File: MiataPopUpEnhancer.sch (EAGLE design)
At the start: 40 parts, among them J3 USB4110-GF-A, Q1 MICRO_COMMERCIAL_MMSS8050-L-T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, Q11 MICRO_COMMERCIAL_MMSS8050-L-T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, Q12 MICRO_COMMERCIAL_MMSS8050-L-T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, Q13 DIODES_INC_DMP3099L-13DIODES_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, Q2 MICRO_COMMERCIAL_MMSS8050-L-T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, Q3 DIODES_INC_DMP3099L-13DIODES_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, SW1 KMR2, U1 ATSAMD21E18A-MUT, U2 MCP1703CB

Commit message: Adds BLE module Adds Motor indicator sense circuitry Simplifies INPUT circuitry for UP/DOWN requests Adds circuit protections
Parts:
- removed J15, J5: (no value), jumper:SJ
- removed J4: (no value), jumper:SJ2W
- added C21, C31, C6: 1uF, adafruit:C-USC0603
- added D13, D23, D3, D33: 3.3V, diode:BZX84CSMD
- added D21, D31: BAT54S, diode:BAT54S
- added D4: BAT54C, diode:BAT54C
- added D5, D6, D7: (no value), adafruit:LEDCHIPLED_0603
- added J22: (no value), adafruit:PINHD-1X6LOCK
- added Q21, Q22, Q31, Q32: MICRO_COMMERCIAL_MMSS8050-L-TPMICRO_COMMERCIAL_MMSS8050-L-T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, Micro Commercial - MMSS8050-L-TP - Copy:MICRO_COMMERCIAL_MMSS8050-L-TPMICRO_COMMERCIAL_MMSS8050-L-TP_0_0
- added Q23, Q33: DIODES_INC_DMP3099L-13DIODES_INC_DMP3099L-13_0_2, Diodes Inc. - DMP3099L-13:DIODES_INC_DMP3099L-13DIODES_INC_DMP3099L-13_0_2
- added R21, R22, R24, R31, R32, R33, R34, R41, R44, R45, S23: 2.2k, rcl:R-US_R0603
- added R25, R35, R42, R43: 100k, rcl:R-US_R0603
- added R26, R36: 1k, rcl:R-US_R0603
- added S1, S11, S21, S31: (no value), jumper:SJ
- added TVS1, TVS2, TVS3, TVS4: ESDU02A5V5R17V, ESDU02A5V5R17V:ESDU02A5V5R17V
- added U3: MDBT40, MDBT40_210701:MDBT40
- added Y1: ABS25-32.768KHZ-T, adafruit:CRYSTALMM20SS
- C1, C11, C4: value 100nF -> 1uF
- D2: value BAT54S -> BAT54C; device diode:BAT54S -> diode:BAT54C
- J1, J2: device adafruit:PINHD-1X8LOCK -> adafruit:PINHD-1X6LOCK
- R1, R11, R12, R2: value 100k -> 2.2k
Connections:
- net DOWN_OUT renamed DOWN_OUT_LH_12V
- removed net +5V: D2.C1A2, J3.VBUS, J3.VBUS_2
- removed net DOWN_OUT_3V3: R14.1
- removed net DOWN_SW: D11.C1A2, J1.5, J15.2, R11.1
- removed net DOWN_SW_3V3: J15.1, Q11.C, R13.1
- removed net DOWN_SW_FILT: C11.1, Q11.B, R11.2, R12.2
- removed net HAZARD: J1.7, J2.7
- removed net LIGHT1: J1.1, J2.1
- removed net LIGHT2: J1.2, J2.2
- removed net UP_OUT: J2.3, Q3.D
- removed net UP_OUT_3V3: R4.1
- removed net UP_SW: D1.C1A2, J1.3, J5.2, R1.1
- removed net UP_SW_3V3: J5.1, Q1.C, R3.1
- removed net UP_SW_FILT: C1.1, Q1.B, R1.2, R2.2
- new net BLE_CONNECTED: R45.1, U3.P0.19
- new net BLE_CTS: R43.1, U1.PA08, U3.P0.10
- new net BLE_MODE: U1.PA02, U3.P0.01
- new net BLE_MODE_LED: R44.1, U3.P0.18
- new net BLE_RTS: U1.PA09, U3.P0.08
- new net BLE_RXD: R42.1, U1.PA06, U3.P0.11
- new net BLE_TXD: U1.PA07, U3.P0.09
- new net DASH_IND_12V: D2.CC, J1.1
- new net DASH_IND_LH: Q21.C, S21.1, S23.1, U1.PA14
- new net DASH_IND_LH_12V: D2.A1, D21.C1A2, J2.1, R21.1
- new net DASH_IND_LH_FILT: C21.1, D23.C, Q21.B, R21.2, R22.2, S21.2
- new net DASH_IND_RH: Q31.C, R33.1, S31.1, U1.PA15
- new net DASH_IND_RH_12V: D2.A2, D31.C1A2, J22.1, R31.1
- new net DASH_IND_RH_FILT: C31.1, D33.C, Q31.B, R31.2, R32.2, S31.2
- new net DEBUG_LED: R41.1, U1.PA10
- new net DOWN_OUT_LH: R14.1, U1.PA18
- new net DOWN_OUT_RH: R34.1, U1.PA16
- new net DOWN_OUT_RH_12V: J22.5, Q33.D
- new net DOWN_REQ: Q11.C, R13.1, S11.1, U1.PA22
- new net DOWN_REQ_12V: D11.C1A2, J1.5, R11.1
- new net DOWN_REQ_FILT: C11.1, D13.C, Q11.B, R11.2, R12.2, S11.2
- new net N$10: Q32.C, Q33.G, R36.1
- new net N$11: Q32.B, R34.2, R35.2
- new net N$12: U3.P0.26/XL2, Y1.2
- new net N$13: U3.P0.27/XL1, Y1.1
- new net N$14: D5.A, R44.2
- new net N$15: D6.A, R45.2
- new net N$16: D7.A, R41.2
- new net N$8: Q22.B, R24.2, R25.2
- new net NC_BLE_FCTRYRST: U3.P0.16
- new net NC_BLE_SWCLK: U3.SWCLK
- new net NC_BLE_SWDIO/RST: U3.NRESET/SWDIO
- new net UP_OUT_LH: R4.1, U1.PA19
- new net UP_OUT_LH_12V: J2.2, Q3.D
- new net UP_OUT_RH: R24.1, U1.PA17
- new net UP_OUT_RH_12V: J22.2, Q23.D
- new net UP_REQ: Q1.C, R3.1, S1.1, U1.PA23
- new net UP_REQ_12V: D1.C1A2, J1.2, R1.1
- new net UP_REQ_FILT: C1.1, D3.C, Q1.B, R1.2, R2.2, S1.2
- new net VBUS: D4.A1, J3.VBUS, J3.VBUS_2, TVS1.2
- new net VIN: C2.1, D4.CC, U2.VI
- net +12V: now also D21.C2, D31.C2, D4.A2, J1.4, J2.4, J22.4, Q23.S, Q33.S, R26.2, R36.2, TVS4.1; no longer C2.1, D2.C2, J2.6, J4.1, U2.VI
- net +3V3: now also C6.1, R33.2, R35.1, R42.2, R43.2, S23.2, U3.AVDD, U3.VDD; no longer J4.3
- net GND: now also C21.2, C31.2, C6.2, D13.A, D21.A1, D23.A, D3.A, D31.A1, D33.A, D5.C, D6.C, D7.C, J1.3, J2.3, J22.3, Q21.E, Q22.E, Q31.E, Q32.E, R22.1, R25.1, R32.1, TVS1.1, TVS2.1, TVS3.1, TVS4.2, U3.GND@1, U3.GND@13, U3.GND@2, U3.GND@25, U3.GND@42, U3.P0.30; no longer J1.8, J2.8
- net N$7: now also Q22.C, Q23.G, R26.1; no longer J1.6, J4.2
- net USB_D+: now also TVS2.2
- net USB_D-: now also TVS3.2
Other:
- note added: "- Figure out wire harness - Determine correct PU/PD polarity for R5 and R15 - Find proper connectors for J1 and J2"
- note added: "1. Zener based: - Populate Dx3 - Nostuff Qx1 and Rx3 - Short Sx1 2. Transistor based (inverted) - Nostuff Dx3 - Populate Qx1 and Rx3 - Open Sx1"
- note added: "BLE module"
- note added: "DASH_IND_LH/RH"
- note added: "From headlight motors"
- note added: "Left"
- note added: "Motor indicators sense"
- note added: "Power regulation"
- note added: "Right"
- note added: "Rx1Cx1 = Rx2Cx1 ~= 2ms"
- note added: "SAMD21 MCU"
- note added: "To Left headlight motor"
- note added: "To Left headlight motor relay"
- note added: "To Right headlight motor"
- note added: "To dash light"
- note added: "UP/DOWN dash switch sense"
- note added: "UP/DOWN_OUT_LH"
- note added: "UP/DOWN_OUT_RH"
- note added: "UP/DOWN_REQ"
- note removed: "- Determine correct PU/PD polarity for R4 and R14 - Find proper connectors for J1 and J2"
- note removed: "Car side"
- note removed: "POWER and MCU"
- note removed: "R11C11 = R12C11 ~= 10ms"
- note removed: "R1C1 = R2C1 ~= 10ms"
- note removed: "Switch side"
- note removed: "To operate the retractor switch at 12V: - Solder J4 pins 1 and 2 - Desolder J4 pins 2 and 3 -/\!\\ Desolder J5, J6 /\!\\ (risk of damage to MCU) - Populate sensing circuitry (Rx1, Cx1, Rx2, Qx1, Rx3)"
- note removed: "To operate the retractor switch at 3.3V: - Solder J4 pins 2 and 3 - Desolder J4 pins 1 and 2 - Solder J5, J6 short - Only populate Rx2"
- note removed: "UP/DOWN switch sense"
- moved on the sheet: C1, C11, C2, C3, C4, C5, D2, J3, R1, R11, R12, R13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

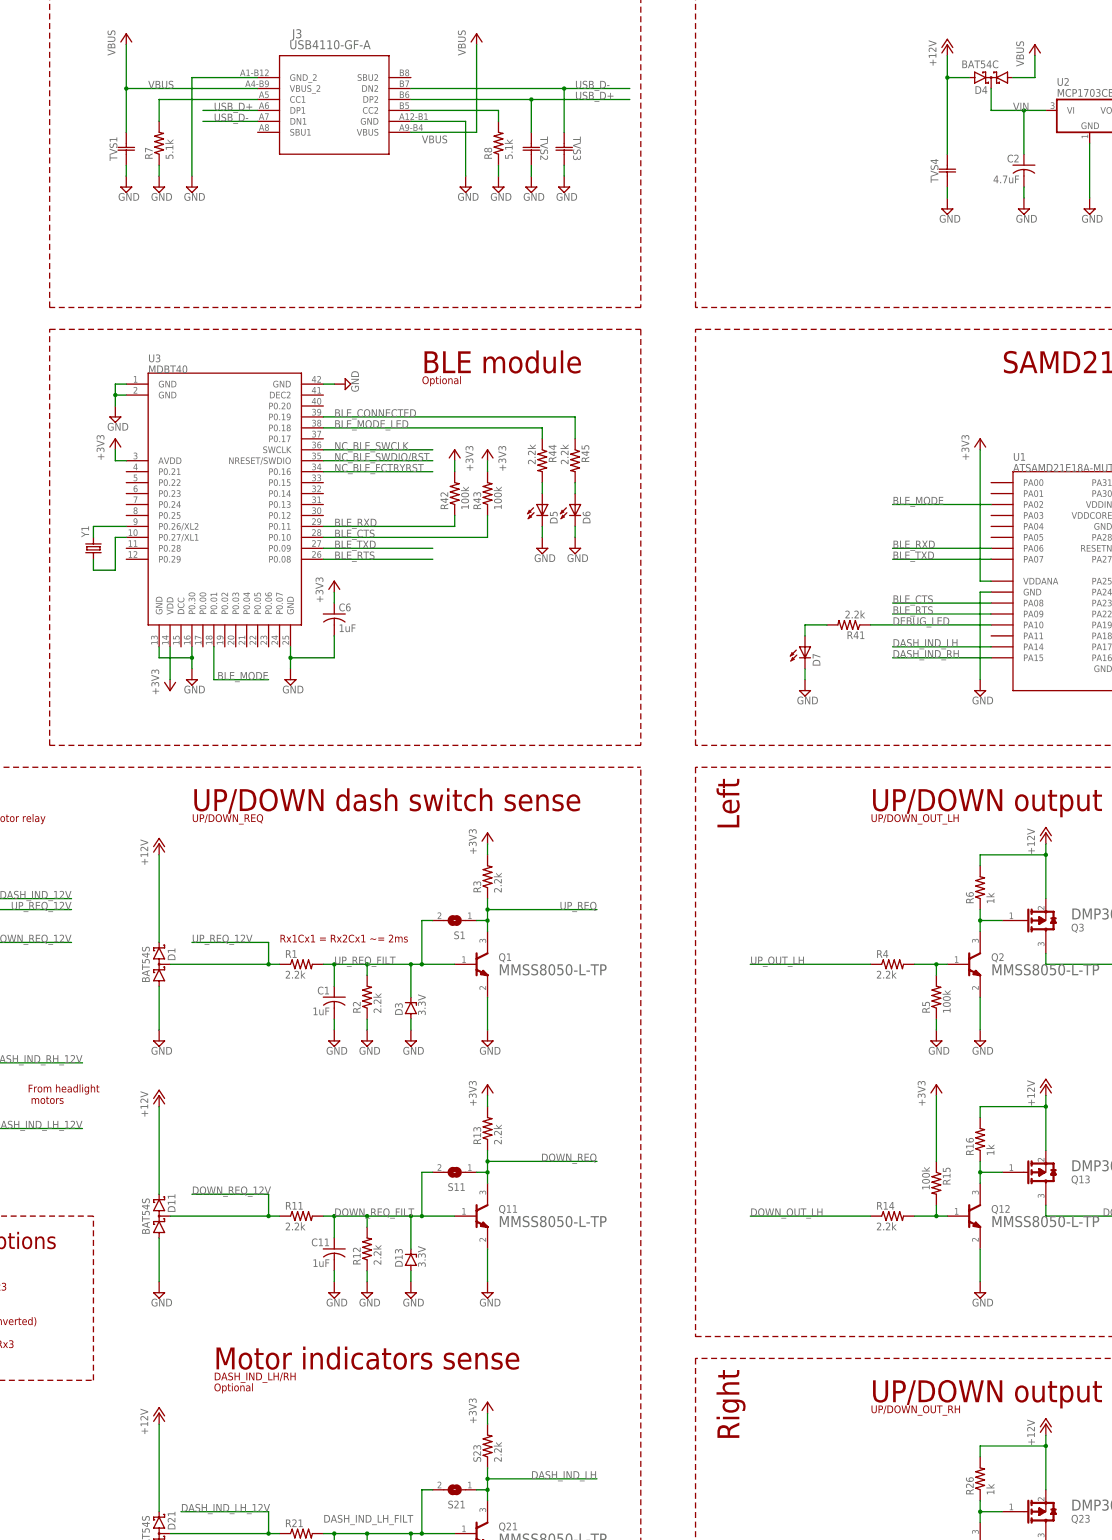
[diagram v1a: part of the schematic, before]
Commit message: Adds first draft of board file. Updates USBC receptable footprint Minor corrections to schematic
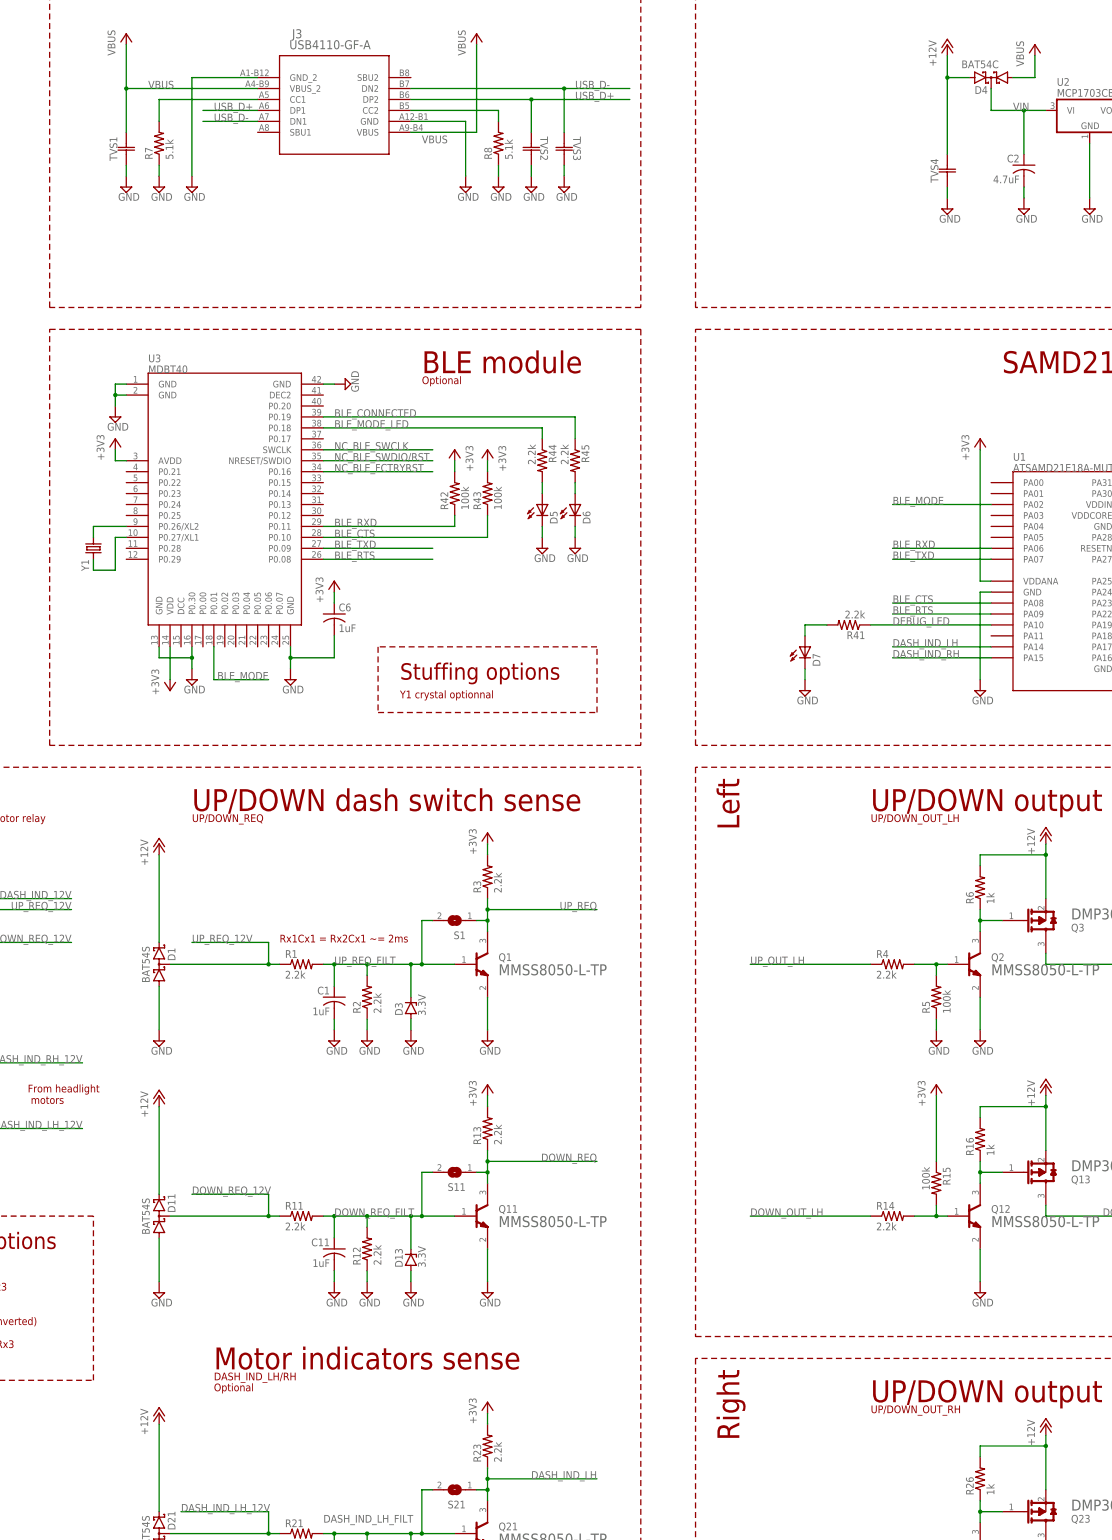
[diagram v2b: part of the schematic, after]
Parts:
- renumbered S23 to R23
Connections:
- net N$3 renamed CC1
- net N$6 renamed CC2
- net N$9 renamed VDDCORE
- removed net N$12: U3.P0.26/XL2, Y1.2
- removed net N$13: U3.P0.27/XL1, Y1.1
- new net XL1: U3.P0.27/XL1, Y1.2
- new net XL2: U3.P0.26/XL2, Y1.1
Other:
- note added: "Y1 crystal optionnal"
- moved on the sheet: Y1
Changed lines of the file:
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@@
 <part name="SUPPLY35" library="supply2" library_urn="urn:adsk.eagle:library:372" deviceset="GND" device=""/>
 <part name="R21" library="rcl" library_urn="urn:adsk.eagle:library:334" deviceset="R-US_" device="R0603" package3d_urn="urn:adsk.eagle:package:23555/3" value="2.2k"/>
-<part name="S23" library="rcl" library_urn="urn:adsk.eagle:library:334" deviceset="R-US_" device="R0603" package3d_urn="urn:adsk.eagle:package:23555/3" value="2.2k"/>
+<part name="R23" library="rcl" library_urn="urn:adsk.eagle:library:334" deviceset="R-US_" device="R0603" package3d_urn="urn:adsk.eagle:package:23555/3" value="2.2k"/>
 <part name="+3V13" library="supply1" library_urn="urn:adsk.eagle:library:371" deviceset="+3V3" device=""/>
 <part name="C21" library="adafruit" deviceset="C-US" device="C0603" value="1uF"/>
@@
 <wire x1="-5.08" y1="-121.92" x2="-55.88" y2="-121.92" width="0.1524" layer="94" style="shortdash"/>
 <text x="22.86" y="-162.56" size="1.778" layer="94">Optional</text>
+<text x="66.04" y="2.54" size="3.81" layer="94">Stuffing options</text>
+<text x="66.04" y="0" size="1.778" layer="94" align="top-left">Y1 crystal optionnal</text>
+<wire x1="60.96" y1="10.16" x2="60.96" y2="-5.08" width="0.1524" layer="94" style="shortdash"/>
+<wire x1="60.96" y1="-5.08" x2="111.76" y2="-5.08" width="0.1524" layer="94" style="shortdash"/>
+<wire x1="111.76" y1="-5.08" x2="111.76" y2="10.16" width="0.1524" layer="94" style="shortdash"/>
+<wire x1="111.76" y1="10.16" x2="60.96" y2="10.16" width="0.1524" layer="94" style="shortdash"/>
 </plain>
 <instances>
@@
 <attribute name="VALUE" x="-2.54" y="53.34" size="1.778" layer="96" rot="R90"/>
 </instance>
-<instance part="Y1" gate="G$1" x="-5.08" y="33.02" smashed="yes" rot="R90">
-<attribute name="NAME" x="-6.096" y="35.56" size="1.778" layer="95" rot="R90"/>
+<instance part="Y1" gate="G$1" x="-5.08" y="33.02" smashed="yes" rot="MR270">
+<attribute name="NAME" x="-6.096" y="30.48" size="1.778" layer="95" rot="MR270"/>
 </instance>
 <instance part="R42" gate="G$1" x="78.74" y="45.72" smashed="yes" rot="R90">
@@
 <attribute name="VALUE" x="39.37" y="-198.882" size="1.778" layer="96"/>
 </instance>
-<instance part="S23" gate="G$1" x="86.36" y="-175.26" smashed="yes" rot="R90">
+<instance part="R23" gate="G$1" x="86.36" y="-175.26" smashed="yes" rot="R90">
 <attribute name="NAME" x="84.8614" y="-179.07" size="1.778" layer="95" rot="R90"/>
 <attribute name="VALUE" x="89.662" y="-179.07" size="1.778" layer="96" rot="R90"/>
@@
 </segment>
 <segment>
-<pinref part="S23" gate="G$1" pin="2"/>
+<pinref part="R23" gate="G$1" pin="2"/>
 <wire x1="86.36" y1="-170.18" x2="86.36" y2="-167.64" width="0.1524" layer="91"/>
 <pinref part="+3V13" gate="G$1" pin="+3V3"/>
@@
 </segment>
 </net>
-<net name="N$9" class="0">
+<net name="VDDCORE" class="0">
 <segment>
 <pinref part="U1" gate="G$1" pin="VDDCORE"/>
@@
 <segment>
 <pinref part="P+2" gate="1" pin="+5V"/>
+<wire x1="213.36" y1="147.32" x2="213.36" y2="142.24" width="0.1524" layer="91"/>
 <pinref part="D4" gate="G$1" pin="A1"/>
-<wire x1="213.36" y1="147.32" x2="213.36" y2="142.24" width="0.1524" layer="91"/>
-<wire x1="213.36" y1="142.24" x2="208.28" y2="142.24" width="0.1524" layer="91"/>
-</segment>
-</net>
-<net name="N$3" class="0">
+<wire x1="208.28" y1="142.24" x2="213.36" y2="142.24" width="0.1524" layer="91"/>
+</segment>
+</net>
+<net name="CC1" class="0">
 <segment>
 <pinref part="R7" gate="G$1" pin="2"/>
@@
 </segment>
 </net>
-<net name="N$6" class="0">
+<net name="CC2" class="0">
 <segment>
 <pinref part="R8" gate="G$1" pin="2"/>
@@
 </segment>
 </net>
-<net name="N$12" class="0">
+<net name="XL2" class="0">
 <segment>
 <pinref part="U3" gate="G$1" pin="P0.26/XL2"/>
 <wire x1="2.54" y1="38.1" x2="-5.08" y2="38.1" width="0.1524" layer="91"/>
-<wire x1="-5.08" y1="38.1" x2="-5.08" y2="35.56" width="0.1524" layer="91"/>
-<pinref part="Y1" gate="G$1" pin="2"/>
-</segment>
-</net>
-<net name="N$13" class="0">
-<segment>
-<wire x1="-5.08" y1="30.48" x2="-5.08" y2="27.94" width="0.1524" layer="91"/>
+<pinref part="Y1" gate="G$1" pin="1"/>
+<wire x1="-5.08" y1="35.56" x2="-5.08" y2="38.1" width="0.1524" layer="91"/>
+</segment>
+</net>
+<net name="XL1" class="0">
+<segment>
 <wire x1="-5.08" y1="27.94" x2="0" y2="27.94" width="0.1524" layer="91"/>
 <wire x1="0" y1="27.94" x2="0" y2="35.56" width="0.1524" layer="91"/>
 <pinref part="U3" gate="G$1" pin="P0.27/XL1"/>
 <wire x1="0" y1="35.56" x2="2.54" y2="35.56" width="0.1524" layer="91"/>
-<pinref part="Y1" gate="G$1" pin="1"/>
+<pinref part="Y1" gate="G$1" pin="2"/>
+<wire x1="-5.08" y1="27.94" x2="-5.08" y2="30.48" width="0.1524" layer="91"/>
 </segment>
 </net>
@@
 <wire x1="86.36" y1="-187.96" x2="86.36" y2="-185.42" width="0.1524" layer="91"/>
 <label x="111.76" y="-182.88" size="1.778" layer="95" rot="MR0"/>
-<pinref part="S23" gate="G$1" pin="1"/>
+<pinref part="R23" gate="G$1" pin="1"/>
 <wire x1="86.36" y1="-185.42" x2="86.36" y2="-182.88" width="0.1524" layer="91"/>
 <wire x1="86.36" y1="-182.88" x2="111.76" y2="-182.88" width="0.1524" layer="91"/>

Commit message: Continues routing and cleanup of south end of board
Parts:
- Q13, Q23, Q3, Q33: value DIODES_INC_DMP3099L-13DIODES_INC_DMP3099L-13_0_2 -> DIODES_INC_DMP3099L-13DIODES_INC_DMP3099L-13_0_0; device Diodes Inc. - DMP3099L-13:DIODES_INC_DMP3099L-13DIODES_INC_DMP3099L-13_0_2 -> Diodes Inc. - DMP3099L-13:DIODES_INC_DMP3099L-13DIODES_INC_DMP3099L-13_0_0
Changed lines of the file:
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@@
 <part name="Q1" library="Micro Commercial - MMSS8050-L-TP - Copy" deviceset="MICRO_COMMERCIAL_MMSS8050-L-TP" device="MICRO_COMMERCIAL_MMSS8050-L-TP_0_0"/>
 <part name="SUPPLY5" library="supply2" library_urn="urn:adsk.eagle:library:372" deviceset="GND" device=""/>
-<part name="Q3" library="Diodes Inc. - DMP3099L-13" deviceset="DIODES_INC_DMP3099L-13" device="DIODES_INC_DMP3099L-13_0_2"/>
+<part name="Q3" library="Diodes Inc. - DMP3099L-13" deviceset="DIODES_INC_DMP3099L-13" device="DIODES_INC_DMP3099L-13_0_0" value="DIODES_INC_DMP3099L-13DIODES_INC_DMP3099L-13_0_0"/>
 <part name="P+4" library="supply1" library_urn="urn:adsk.eagle:library:371" deviceset="+12V" device=""/>
 <part name="R6" library="rcl" library_urn="urn:adsk.eagle:library:334" deviceset="R-US_" device="R0603" package3d_urn="urn:adsk.eagle:package:23555/3" value="1k"/>
@@
 <part name="R3" library="rcl" library_urn="urn:adsk.eagle:library:334" deviceset="R-US_" device="R0603" package3d_urn="urn:adsk.eagle:package:23555/3" value="2.2k"/>
 <part name="+3V3" library="supply1" library_urn="urn:adsk.eagle:library:371" deviceset="+3V3" device=""/>
-<part name="Q13" library="Diodes Inc. - DMP3099L-13" deviceset="DIODES_INC_DMP3099L-13" device="DIODES_INC_DMP3099L-13_0_2"/>
+<part name="Q13" library="Diodes Inc. - DMP3099L-13" deviceset="DIODES_INC_DMP3099L-13" device="DIODES_INC_DMP3099L-13_0_0" value="DIODES_INC_DMP3099L-13DIODES_INC_DMP3099L-13_0_0"/>
 <part name="P+3" library="supply1" library_urn="urn:adsk.eagle:library:371" deviceset="+12V" device=""/>
 <part name="R16" library="rcl" library_urn="urn:adsk.eagle:library:334" deviceset="R-US_" device="R0603" package3d_urn="urn:adsk.eagle:package:23555/3" value="1k"/>
@@
 <part name="SUPPLY29" library="supply2" library_urn="urn:adsk.eagle:library:372" deviceset="GND" device=""/>
 <part name="SUPPLY30" library="supply2" library_urn="urn:adsk.eagle:library:372" deviceset="GND" device=""/>
-<part name="Q23" library="Diodes Inc. - DMP3099L-13" deviceset="DIODES_INC_DMP3099L-13" device="DIODES_INC_DMP3099L-13_0_2"/>
+<part name="Q23" library="Diodes Inc. - DMP3099L-13" deviceset="DIODES_INC_DMP3099L-13" device="DIODES_INC_DMP3099L-13_0_0" value="DIODES_INC_DMP3099L-13DIODES_INC_DMP3099L-13_0_0"/>
 <part name="P+11" library="supply1" library_urn="urn:adsk.eagle:library:371" deviceset="+12V" device=""/>
 <part name="R26" library="rcl" library_urn="urn:adsk.eagle:library:334" deviceset="R-US_" device="R0603" package3d_urn="urn:adsk.eagle:package:23555/3" value="1k"/>
@@
 <part name="SUPPLY34" library="supply2" library_urn="urn:adsk.eagle:library:372" deviceset="GND" device=""/>
 <part name="R24" library="rcl" library_urn="urn:adsk.eagle:library:334" deviceset="R-US_" device="R0603" package3d_urn="urn:adsk.eagle:package:23555/3" value="2.2k"/>
-<part name="Q33" library="Diodes Inc. - DMP3099L-13" deviceset="DIODES_INC_DMP3099L-13" device="DIODES_INC_DMP3099L-13_0_2"/>
+<part name="Q33" library="Diodes Inc. - DMP3099L-13" deviceset="DIODES_INC_DMP3099L-13" device="DIODES_INC_DMP3099L-13_0_0" value="DIODES_INC_DMP3099L-13DIODES_INC_DMP3099L-13_0_0"/>
 <part name="P+12" library="supply1" library_urn="urn:adsk.eagle:library:371" deviceset="+12V" device=""/>
 <part name="R36" library="rcl" library_urn="urn:adsk.eagle:library:334" deviceset="R-US_" device="R0603" package3d_urn="urn:adsk.eagle:package:23555/3" value="1k"/>
